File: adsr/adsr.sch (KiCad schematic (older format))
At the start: 11 parts, among them J1 B_GATE, J2 A_GATE, J3 B_IN, J4 A_IN, J5 B_OUT, J6 A_OUT, J7 EURORACK_CONN_16, J8 Conn_01x04_Male, U1 LM13700

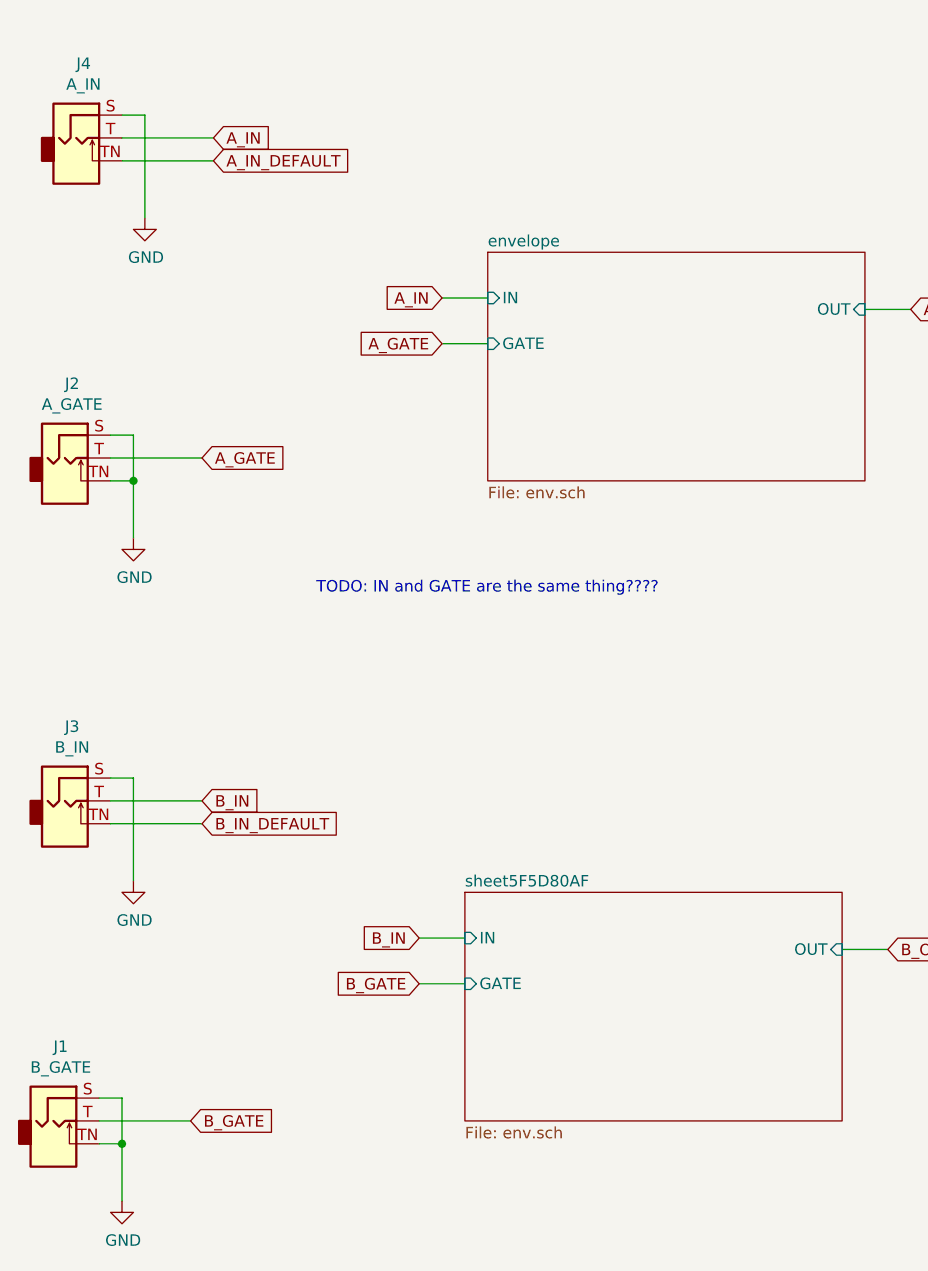
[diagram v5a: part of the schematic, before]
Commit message: reduce to one input
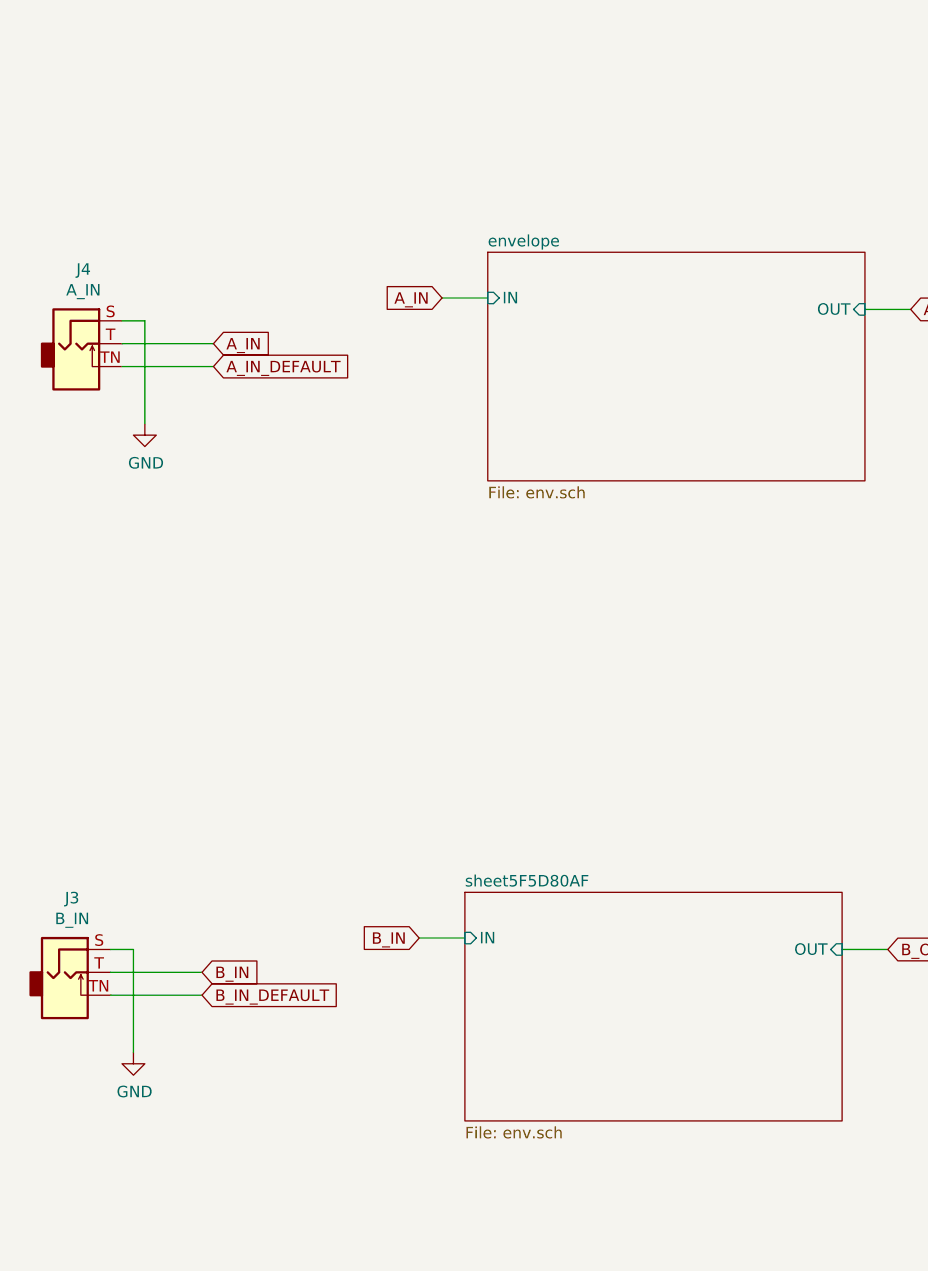
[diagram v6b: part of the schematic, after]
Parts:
- removed J1: B_GATE, synth:Jack_3.5mm_QingPu_WQP-PJ398SM_Vertical_CircularHoles, symbol Connector:AudioJack2_SwitchT
- removed J2: A_GATE, synth:Jack_3.5mm_QingPu_WQP-PJ398SM_Vertical_CircularHoles, symbol Connector:AudioJack2_SwitchT
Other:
- note removed: "TODO: IN and GATE are the same thing????"
- moved on the sheet: J3, J4
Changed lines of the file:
@@
 Wire Wire Line
 	10400 1000 10400 850
-Text GLabel 1600 1100 2    50   Input ~ 0
+Text GLabel 1600 2000 2    50   Input ~ 0
 A_IN
 Wire Wire Line
-	1600 1100 1200 1100
+	1600 2000 1200 2000
 $Comp
 L power:GND #PWR04
 U 1 1 5F337BC4
-P 1300 1450
-F 0 "#PWR04" H 1300 1200 50  0001 C CNN
-F 1 "GND" H 1305 1277 50  0000 C CNN
-F 2 "" H 1300 1450 50  0001 C CNN
-F 3 "" H 1300 1450 50  0001 C CNN
-	1    1300 1450
-	1    0    0    -1
-$EndComp
-Wire Wire Line
-	1200 1000 1300 1000
-Wire Wire Line
-	1300 1000 1300 1450
-Text GLabel 1600 1200 2    50   Input ~ 0
+P 1300 2350
+F 0 "#PWR04" H 1300 2100 50  0001 C CNN
+F 1 "GND" H 1305 2177 50  0000 C CNN
+F 2 "" H 1300 2350 50  0001 C CNN
+F 3 "" H 1300 2350 50  0001 C CNN
+	1    1300 2350
+	1    0    0    -1
+$EndComp
+Wire Wire Line
+	1200 1900 1300 1900
+Wire Wire Line
+	1300 1900 1300 2350
+Text GLabel 1600 2100 2    50   Input ~ 0
 A_IN_DEFAULT
 Wire Wire Line
-	1600 1200 1200 1200
-Wire Wire Line
-	1550 2500 1150 2500
-$Comp
-L power:GND #PWR02
-U 1 1 5F3462D1
-P 1250 2850
-F 0 "#PWR02" H 1250 2600 50  0001 C CNN
-F 1 "GND" H 1255 2677 50  0000 C CNN
-F 2 "" H 1250 2850 50  0001 C CNN
-F 3 "" H 1250 2850 50  0001 C CNN
-	1    1250 2850
-	1    0    0    -1
-$EndComp
-Wire Wire Line
-	1150 2400 1250 2400
-Wire Wire Line
-	1250 2400 1250 2600
-Wire Wire Line
-	1150 2600 1250 2600
-Connection ~ 1250 2600
-Wire Wire Line
-	1250 2600 1250 2850
-Text GLabel 1550 2500 2    50   Input ~ 0
-A_GATE
+	1600 2100 1200 2100
 Wire Wire Line
 	6000 1950 6400 1950
@@
 F1 "env.sch" 50
 F2 "IN" I L 2800 1800 50
-F3 "GATE" I L 2800 2000 50
-F4 "OUT" I R 4450 1850 50
+F3 "OUT" I R 4450 1850 50
 $EndSheet
-Text GLabel 2600 2000 0    50   Input ~ 0
-A_GATE
 Text GLabel 2600 1800 0    50   Input ~ 0
 A_IN
 Wire Wire Line
 	2600 1800 2800 1800
-Wire Wire Line
-	2800 2000 2600 2000
 Text GLabel 4650 1850 2    50   Input ~ 0
 A_OUT
@@
 F1 "env.sch" 50
 F2 "IN" I L 2700 4600 50
-F3 "GATE" I L 2700 4800 50
-F4 "OUT" I R 4350 4650 50
+F3 "OUT" I R 4350 4650 50
 $EndSheet
-Text GLabel 2500 4800 0    50   Input ~ 0
-B_GATE
 Text GLabel 2500 4600 0    50   Input ~ 0
 B_IN
 Wire Wire Line
 	2500 4600 2700 4600
-Wire Wire Line
-	2700 4800 2500 4800
 Text GLabel 4550 4650 2    50   Input ~ 0
 B_OUT
 Wire Wire Line
 	4550 4650 4350 4650
-Text GLabel 1550 4000 2    50   Input ~ 0
+Text GLabel 1550 4750 2    50   Input ~ 0
 B_IN
 Wire Wire Line
-	1550 4000 1150 4000
+	1550 4750 1150 4750
 $Comp
 L power:GND #PWR03
 U 1 1 5F5DAD34
-P 1250 4350
-F 0 "#PWR03" H 1250 4100 50  0001 C CNN
-F 1 "GND" H 1255 4177 50  0000 C CNN
-F 2 "" H 1250 4350 50  0001 C CNN
-F 3 "" H 1250 4350 50  0001 C CNN
-	1    1250 4350
-	1    0    0    -1
-$EndComp
-Wire Wire Line
-	1150 3900 1250 3900
-Wire Wire Line
-	1250 3900 1250 4350
-Text GLabel 1550 4100 2    50   Input ~ 0
+P 1250 5100
+F 0 "#PWR03" H 1250 4850 50  0001 C CNN
+F 1 "GND" H 1255 4927 50  0000 C CNN
+F 2 "" H 1250 5100 50  0001 C CNN
+F 3 "" H 1250 5100 50  0001 C CNN
+	1    1250 5100
+	1    0    0    -1
+$EndComp
+Wire Wire Line
+	1150 4650 1250 4650
+Wire Wire Line
+	1250 4650 1250 5100
+Text GLabel 1550 4850 2    50   Input ~ 0
 B_IN_DEFAULT
 Wire Wire Line
-	1550 4100 1150 4100
-Wire Wire Line
-	1500 5400 1100 5400
-$Comp
-L power:GND #PWR01
-U 1 1 5F5DAD54
-P 1200 5750
-F 0 "#PWR01" H 1200 5500 50  0001 C CNN
-F 1 "GND" H 1205 5577 50  0000 C CNN
-F 2 "" H 1200 5750 50  0001 C CNN
-F 3 "" H 1200 5750 50  0001 C CNN
-	1    1200 5750
-	1    0    0    -1
-$EndComp
-Wire Wire Line
-	1100 5300 1200 5300
-Wire Wire Line
-	1200 5300 1200 5500
-Wire Wire Line
-	1100 5500 1200 5500
-Connection ~ 1200 5500
-Wire Wire Line
-	1200 5500 1200 5750
-Text GLabel 1500 5400 2    50   Input ~ 0
-B_GATE
+	1550 4850 1150 4850
 Wire Wire Line
 	5650 4950 6050 4950
@@
 L Connector:AudioJack2_SwitchT J4
 U 1 1 6146D779
-P 1000 1100
-F 0 "J4" H 1032 1425 50  0000 C CNN
-F 1 "A_IN" H 1032 1334 50  0000 C CNN
-F 2 "synth:Jack_3.5mm_QingPu_WQP-PJ398SM_Vertical_CircularHoles" H 1000 1100 50  0001 C CNN
-F 3 "~" H 1000 1100 50  0001 C CNN
-	1    1000 1100
-	1    0    0    -1
-$EndComp
-$Comp
-L Connector:AudioJack2_SwitchT J2
-U 1 1 6146FC09
-P 950 2500
-F 0 "J2" H 982 2825 50  0000 C CNN
-F 1 "A_GATE" H 982 2734 50  0000 C CNN
-F 2 "synth:Jack_3.5mm_QingPu_WQP-PJ398SM_Vertical_CircularHoles" H 950 2500 50  0001 C CNN
-F 3 "~" H 950 2500 50  0001 C CNN
-	1    950  2500
+P 1000 2000
+F 0 "J4" H 1032 2325 50  0000 C CNN
+F 1 "A_IN" H 1032 2234 50  0000 C CNN
+F 2 "synth:Jack_3.5mm_QingPu_WQP-PJ398SM_Vertical_CircularHoles" H 1000 2000 50  0001 C CNN
+F 3 "~" H 1000 2000 50  0001 C CNN
+	1    1000 2000
 	1    0    0    -1
 $EndComp
@@
 L Connector:AudioJack2_SwitchT J3
 U 1 1 61470257
-P 950 4000
-F 0 "J3" H 982 4325 50  0000 C CNN
-F 1 "B_IN" H 982 4234 50  0000 C CNN
-F 2 "synth:Jack_3.5mm_QingPu_WQP-PJ398SM_Vertical_CircularHoles" H 950 4000 50  0001 C CNN
-F 3 "~" H 950 4000 50  0001 C CNN
-	1    950  4000
-	1    0    0    -1
-$EndComp
-$Comp
-L Connector:AudioJack2_SwitchT J1
-U 1 1 61470A7A
-P 900 5400
-F 0 "J1" H 932 5725 50  0000 C CNN
-F 1 "B_GATE" H 932 5634 50  0000 C CNN
-F 2 "synth:Jack_3.5mm_QingPu_WQP-PJ398SM_Vertical_CircularHoles" H 900 5400 50  0001 C CNN
-F 3 "~" H 900 5400 50  0001 C CNN
-	1    900  5400
+P 950 4750
+F 0 "J3" H 982 5075 50  0000 C CNN
+F 1 "B_IN" H 982 4984 50  0000 C CNN
+F 2 "synth:Jack_3.5mm_QingPu_WQP-PJ398SM_Vertical_CircularHoles" H 950 4750 50  0001 C CNN
+F 3 "~" H 950 4750 50  0001 C CNN
+	1    950  4750
 	1    0    0    -1
 $EndComp
@@
 Text Notes 7600 1850 0    50   ~ 0
 Bypass capacitors for LM13700
-Text Notes 2050 3100 0    50   ~ 0
-TODO: IN and GATE are the same thing????
 $EndSCHEMATC

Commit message: adsr improvements
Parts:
- added C1, C3: 0.1u, Capacitor_SMD:C_1206_3216Metric_Pad1.42x1.75mm_HandSolder, symbol Device:C
- added J1: Conn_01x04_Female, Connector_PinHeader_2.54mm:PinHeader_1x04_P2.54mm_Vertical, symbol Connector:Conn_01x04_Female
- added J13, J14, J2: Conn_01x04_Male, Connector_PinHeader_2.54mm:PinHeader_1x04_P2.54mm_Vertical, symbol Connector:Conn_01x04_Male
- added U8: TL072, Package_DIP:DIP-8_W7.62mm, symbol Amplifier_Operational:TL072
- J8: footprint Connector_PinHeader_2.54mm:PinHeader_2x02_P2.54mm_Vertical -> Connector_PinHeader_2.54mm:PinHeader_1x04_P2.54mm_Vertical
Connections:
- net +12V: now also C1.1, J1.2 (Pin_2), J14.3 (Pin_3), U8.8 (V+)
- net +5V: now also J1.1 (Pin_1), J14.4 (Pin_4)
- net -12V: now also C3.2, J1.4 (Pin_4), J14.1 (Pin_1), U8.4 (V-)
- net A_IN_DEFAULT: now also J8.3 (Pin_3), J13.3 (Pin_3), J2.3 (Pin_3); no longer J8.1 (Pin_1)
- net A_OUT_DEFAULT: now also J8.4 (Pin_4), J13.4 (Pin_4), J2.4 (Pin_4); no longer J8.3 (Pin_3)
- net B_IN_DEFAULT: now also J13.2 (Pin_2), J2.2 (Pin_2)
- net B_OUT_DEFAULT: now also J8.1 (Pin_1), J13.1 (Pin_1), J2.1 (Pin_1); no longer J8.4 (Pin_4)
- net GND: now also C1.2, C3.1, J1.3 (Pin_3), J14.2 (Pin_2)
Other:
- note added: "Gotta pass this through 3 boards"
- note added: "ceramic bypass capacitors for TL072\nclose to power supply pins"
- note added: "power supply interconnect"
- moved on the sheet: J4, J6
